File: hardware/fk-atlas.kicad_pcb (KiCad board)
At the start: 2 copper layers, 88.4 x 80.3 mm, 127 parts, among them J1 CONN-HDR-2x5, J2 MICRO-USB, J201 CONN_01X02, J3 Conn_01x02, J301 CONN_01X02, J4 Conn_01x07, J401 CONN_01X02, J501 CONN_01X02, J601 CONN_01X02, P2 ATLAS_EC_PROBE, P3 ATLAS_RTD_PROBE, P4 ATLAS_PH_PROBE, P5 ATLAS_DO_PROBE, P6 ATLAS_ORP_PROBE, Q1 2N7002LT1G, Q2 2N7002LT1G, Q3 2N7002LT1G, Q4 2N7002LT1G, Q5 2N7002LT1G, SW1 SPNO, U1 S25FL1xxK0XM, U2 ATSAMD21G18A-AU, U201 ADM3260, U202 ATLAS_EC, U3 MCP1700T-3302E/MB, U301 ADM3260, U302 ATLAS_RTD, U401 ADM3260, U402 ATLAS_PH, U501 ADM3260, U502 ATLAS_DO, U601 ADM3260, U602 ATLAS_ORP, Y1 FC-135

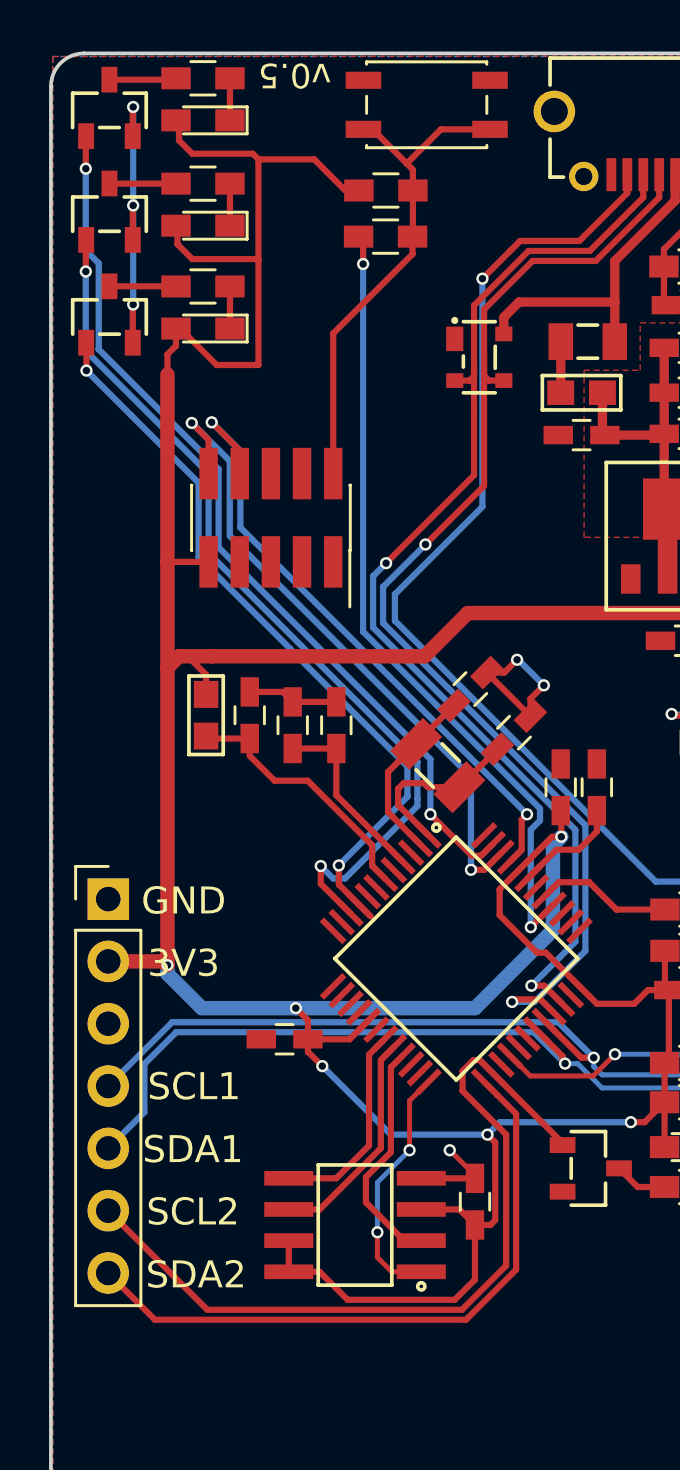
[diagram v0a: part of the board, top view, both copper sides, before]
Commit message: Break out Wire3 instead of Wire2.
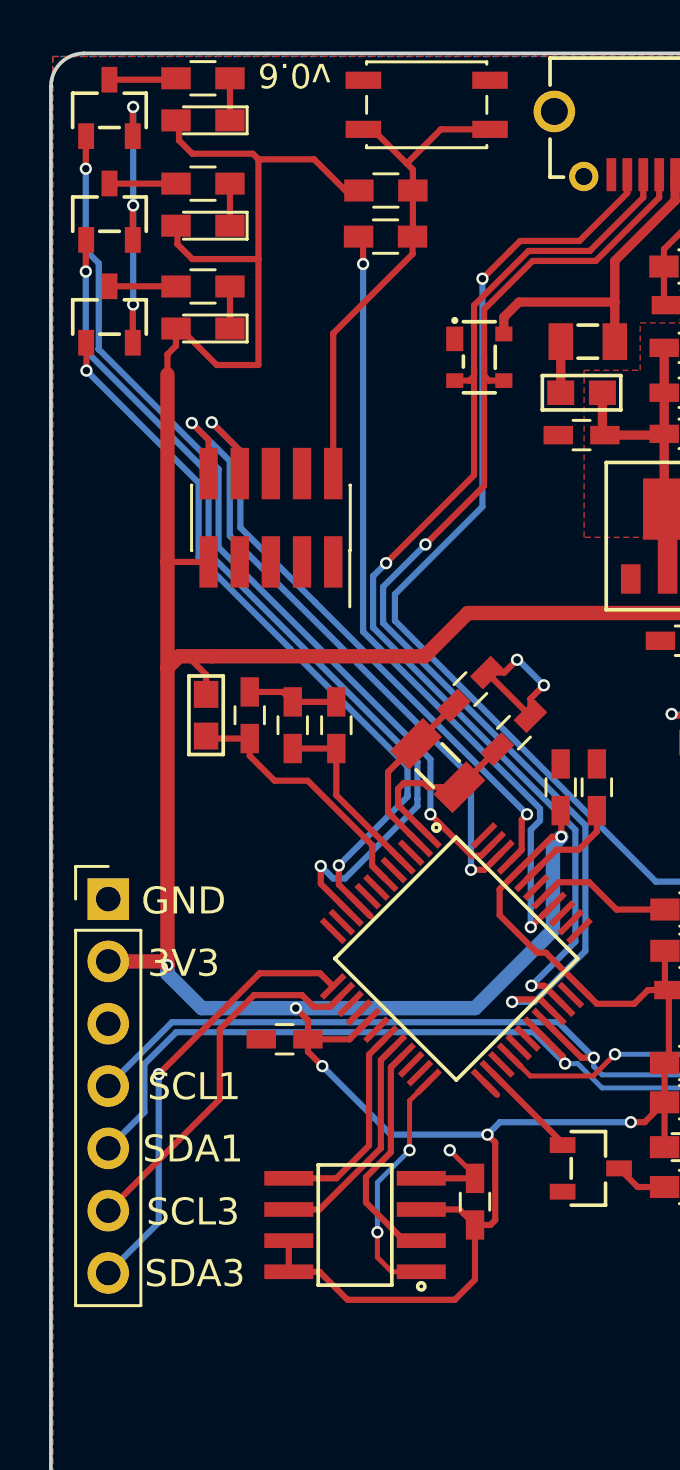
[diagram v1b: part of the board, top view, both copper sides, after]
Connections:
- net /D5 renamed /FLASH_CS
- net /SCL renamed /SCL1
- net /SDA renamed /SDA1
- J4 pad 6: /D13 -> /SCL3
- J4 pad 7: /D11 -> /SDA3
- U2 pad 13: /D4 -> /SDA3
- U2 pad 14: /D3 -> /SCL3
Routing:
- net /D13: track 33.0 -> 4.11 mm
- net /D11: track 26.5 -> 0.75 mm
- net /SDA3: track 0.00 -> 18.0 mm, vias 0 -> 1
- net /SCL3: track 0.00 -> 15.2 mm
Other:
- board text added: "SCL3"
- board text added: "SDA3"
- board text added: "v0.6"
- board text removed: "SCL2"
- board text removed: "SDA2"
- board text removed: "v0.5"

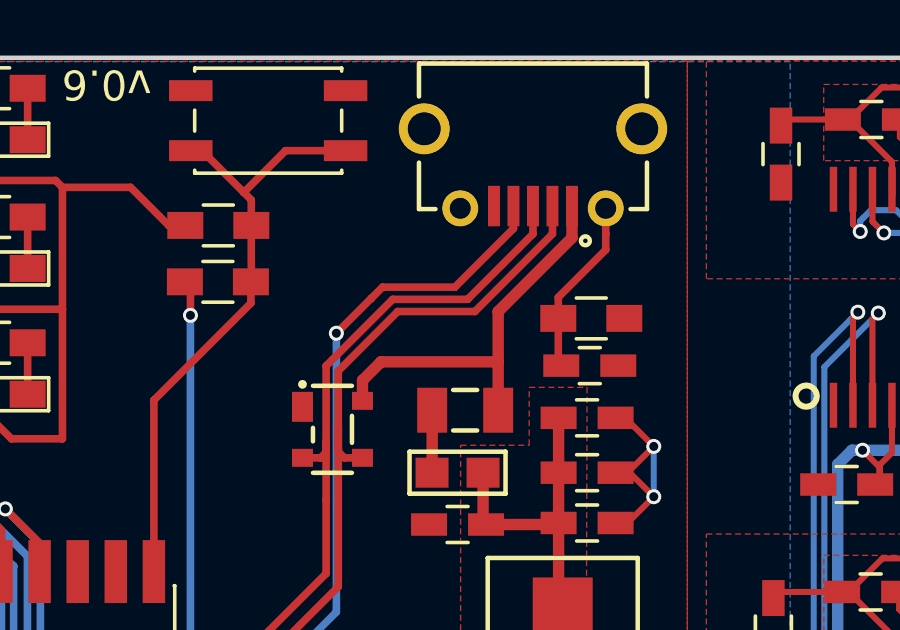
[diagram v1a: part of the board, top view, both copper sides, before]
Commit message: Give GND on USB a firmer connection.
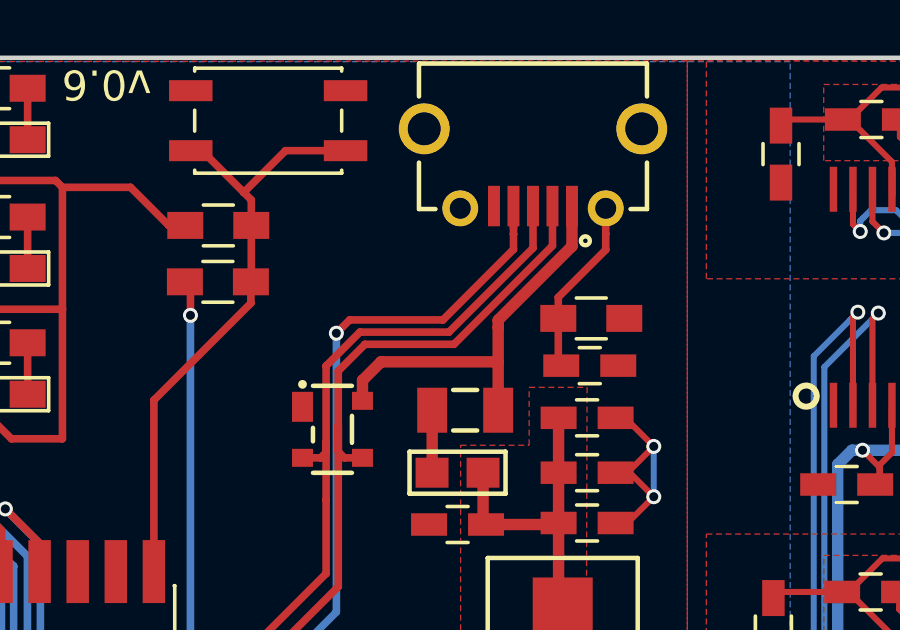
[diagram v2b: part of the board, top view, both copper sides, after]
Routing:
- net Net-(J2-Pad4): track 43.9 -> 45.1 mm
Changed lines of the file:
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@@
     (links 348)
     (no_connects 0)
-    (area 115.672799 57.328999 204.214801 137.743001)
+    (area 106.559933 55.6511 223.731401 137.9054)
     (thickness 1.6)
     (drawings 25)
-    (tracks 1150)
+    (tracks 1152)
     (zones 0)
     (modules 127)
@@
   )
   (setup
-    (last_trace_width 0.254)
+    (last_trace_width 0.381)
     (user_trace_width 0.203)
     (user_trace_width 0.381)
@@
   (segment (start 123.0454 64.4271) (end 123.0454 62.4381) (width 0.254) (layer F.Cu) (net 56))
   (segment (start 123.0454 60.1345) (end 123.0454 58.42) (width 0.254) (layer F.Cu) (net 57))
+  (segment (start 139.8905 62.3465) (end 139.8905 63.746597) (width 0.254) (layer F.Cu) (net 58))
+  (segment (start 139.8905 63.746597) (end 137.089107 66.54799) (width 0.254) (layer F.Cu) (net 58))
+  (segment (start 137.089107 66.54799) (end 134.12146 66.54799) (width 0.254) (layer F.Cu) (net 58))
+  (segment (start 134.12146 66.54799) (end 132.99439 67.67506) (width 0.254) (layer F.Cu) (net 58))
+  (segment (start 132.99439 67.67506) (end 132.99439 70.2056) (width 0.254) (layer F.Cu) (net 58))
   (segment (start 135.3312 95.4024) (end 137.123309 93.610291) (width 0.254) (layer B.Cu) (net 58))
   (segment (start 137.123309 93.610291) (end 137.123309 89.050559) (width 0.254) (layer B.Cu) (net 58))
@@
   (segment (start 135.850273 95.4024) (end 135.3312 95.4024) (width 0.254) (layer F.Cu) (net 58))
   (via (at 135.3312 95.4024) (size 0.5) (drill 0.3) (layers F.Cu B.Cu) (net 58))
-  (segment (start 132.99439 67.67506) (end 132.99439 70.2056) (width 0.254) (layer F.Cu) (net 58))
   (segment (start 132.99439 70.2056) (end 132.99439 72.13599) (width 0.254) (layer F.Cu) (net 58))
   (segment (start 132.207 70.739) (end 132.811 70.739) (width 0.254) (layer F.Cu) (net 58))
@@
   (segment (start 132.99439 74.59582) (end 129.40901 78.1812) (width 0.254) (layer F.Cu) (net 58))
   (via (at 129.40901 78.1812) (size 0.5) (drill 0.3) (layers F.Cu B.Cu) (net 58))
-  (segment (start 139.8905 62.3465) (end 139.8905 63.2755) (width 0.254) (layer F.Cu) (net 58))
-  (segment (start 139.8905 63.2755) (end 137.71021 65.45579) (width 0.254) (layer F.Cu) (net 58))
-  (segment (start 137.71021 65.45579) (end 135.213659 65.455791) (width 0.254) (layer F.Cu) (net 58))
-  (segment (start 135.213659 65.455791) (end 132.99439 67.67506) (width 0.254) (layer F.Cu) (net 58))
+  (segment (start 140.5405 62.3465) (end 140.5405 63.671347) (width 0.254) (layer F.Cu) (net 59))
+  (segment (start 140.5405 63.671347) (end 137.257448 66.9544) (width 0.254) (layer F.Cu) (net 59))
+  (segment (start 137.257448 66.9544) (end 134.2898 66.9544) (width 0.254) (layer F.Cu) (net 59))
+  (segment (start 134.2898 66.9544) (end 133.4008 67.8434) (width 0.254) (layer F.Cu) (net 59))
+  (segment (start 133.4008 67.8434) (end 133.4008 69.6722) (width 0.254) (layer F.Cu) (net 59))
   (segment (start 131.0132 77.4192) (end 129.28602 79.14638) (width 0.254) (layer B.Cu) (net 59))
   (segment (start 137.529719 88.863319) (end 137.529719 93.987395) (width 0.254) (layer B.Cu) (net 59))
@@
   (via (at 134.5438 96.0628) (size 0.5) (drill 0.3) (layers F.Cu B.Cu) (net 59))
   (segment (start 133.4008 75.0316) (end 133.4008 69.6722) (width 0.254) (layer F.Cu) (net 59))
-  (segment (start 133.4008 69.6722) (end 133.4008 67.8434) (width 0.254) (layer F.Cu) (net 59))
   (segment (start 134.207 70.739) (end 133.603 70.739) (width 0.254) (layer F.Cu) (net 59))
   (segment (start 133.603 70.739) (end 133.4008 70.5368) (width 0.254) (layer F.Cu) (net 59))
   (segment (start 133.4008 70.5368) (end 133.4008 69.6722) (width 0.254) (layer F.Cu) (net 59))
   (segment (start 131.0132 77.4192) (end 133.4008 75.0316) (width 0.254) (layer F.Cu) (net 59))
-  (segment (start 133.4008 67.8434) (end 135.382 65.8622) (width 0.254) (layer F.Cu) (net 59))
-  (segment (start 140.5405 63.2755) (end 140.5405 62.3465) (width 0.254) (layer F.Cu) (net 59))
-  (segment (start 135.382 65.8622) (end 137.9538 65.8622) (width 0.254) (layer F.Cu) (net 59))
-  (segment (start 137.9538 65.8622) (end 140.5405 63.2755) (width 0.254) (layer F.Cu) (net 59))
   (via (at 131.0132 77.4192) (size 0.5) (drill 0.3) (layers F.Cu B.Cu) (net 59))
+  (segment (start 141.1905 62.3465) (end 141.1905 63.6859) (width 0.381) (layer F.Cu) (net 60))
+  (segment (start 141.1905 63.6859) (end 138.7299 66.1465) (width 0.381) (layer F.Cu) (net 60))
+  (segment (start 138.7299 66.1465) (end 138.7299 66.3956) (width 0.381) (layer F.Cu) (net 60))
+  (segment (start 138.7299 66.3956) (end 138.7299 67.5386) (width 0.381) (layer F.Cu) (net 60))
   (segment (start 134.207 68.158) (end 134.8264 67.5386) (width 0.381) (layer F.Cu) (net 60))
-  (segment (start 138.7299 65.8631) (end 138.7299 67.5386) (width 0.381) (layer F.Cu) (net 60))
   (segment (start 138.7299 67.5386) (end 138.7299 69.1515) (width 0.381) (layer F.Cu) (net 60))
   (segment (start 134.8264 67.5386) (end 138.7299 67.5386) (width 0.381) (layer F.Cu) (net 60))
   (segment (start 134.207 68.839) (end 134.207 68.158) (width 0.381) (layer F.Cu) (net 60))
-  (segment (start 141.1905 62.3465) (end 141.1905 63.4025) (width 0.381) (layer F.Cu) (net 60))
-  (segment (start 141.1905 63.4025) (end 138.7299 65.8631) (width 0.381) (layer F.Cu) (net 60))
   (segment (start 136.5299 69.1515) (end 136.5299 71.2303) (width 0.381) (layer F.Cu) (net 61))
   (segment (start 136.5299 71.2303) (end 136.5259 71.2343) (width 0.381) (layer F.Cu) (net 61))
@@
   (segment (start 128.859 60.4995) (end 130.2512 61.8917) (width 0.254) (layer F.Cu) (net 65))
   (segment (start 130.2512 64.858) (end 130.2376 64.8716) (width 0.254) (layer F.Cu) (net 65))
+  (segment (start 133.335982 66.584782) (end 133.779184 66.14158) (width 0.254) (layer F.Cu) (net 66))
+  (segment (start 133.779184 66.14158) (end 136.89007 66.14158) (width 0.254) (layer F.Cu) (net 66))
+  (segment (start 136.89007 66.14158) (end 139.2405 63.79115) (width 0.254) (layer F.Cu) (net 66))
+  (segment (start 139.2405 63.79115) (end 139.2405 63.2755) (width 0.254) (layer F.Cu) (net 66))
+  (segment (start 139.2405 62.3465) (end 139.2405 63.2755) (width 0.254) (layer F.Cu) (net 66))
+  (segment (start 139.2405 63.2755) (end 139.2428 63.2778) (width 0.254) (layer F.Cu) (net 66))
   (segment (start 142.9512 91.1606) (end 140.40175 91.1606) (width 0.254) (layer B.Cu) (net 66))
   (segment (start 140.40175 91.1606) (end 129.7686 80.52745) (width 0.254) (layer B.Cu) (net 66))
@@
   (segment (start 129.7686 79.447314) (end 133.335982 75.879932) (width 0.254) (layer B.Cu) (net 66))
   (segment (start 133.335982 75.879932) (end 133.335982 66.584782) (width 0.254) (layer B.Cu) (net 66))
-  (segment (start 133.335982 66.584782) (end 134.490364 65.4304) (width 0.254) (layer F.Cu) (net 66))
-  (segment (start 134.490364 65.4304) (end 134.492982 65.4304) (width 0.254) (layer F.Cu) (net 66))
-  (segment (start 134.492982 65.4304) (end 134.874 65.049382) (width 0.254) (layer F.Cu) (net 66))
-  (segment (start 134.874 65.049382) (end 137.287018 65.049382) (width 0.254) (layer F.Cu) (net 66))
-  (segment (start 137.287018 65.049382) (end 139.2405 63.0959) (width 0.254) (layer F.Cu) (net 66))
   (segment (start 139.2405 63.0959) (end 139.2405 62.3465) (width 0.254) (layer F.Cu) (net 66))
   (via (at 133.335982 66.584782) (size 0.5) (drill 0.3) (layers F.Cu B.Cu) (net 66))

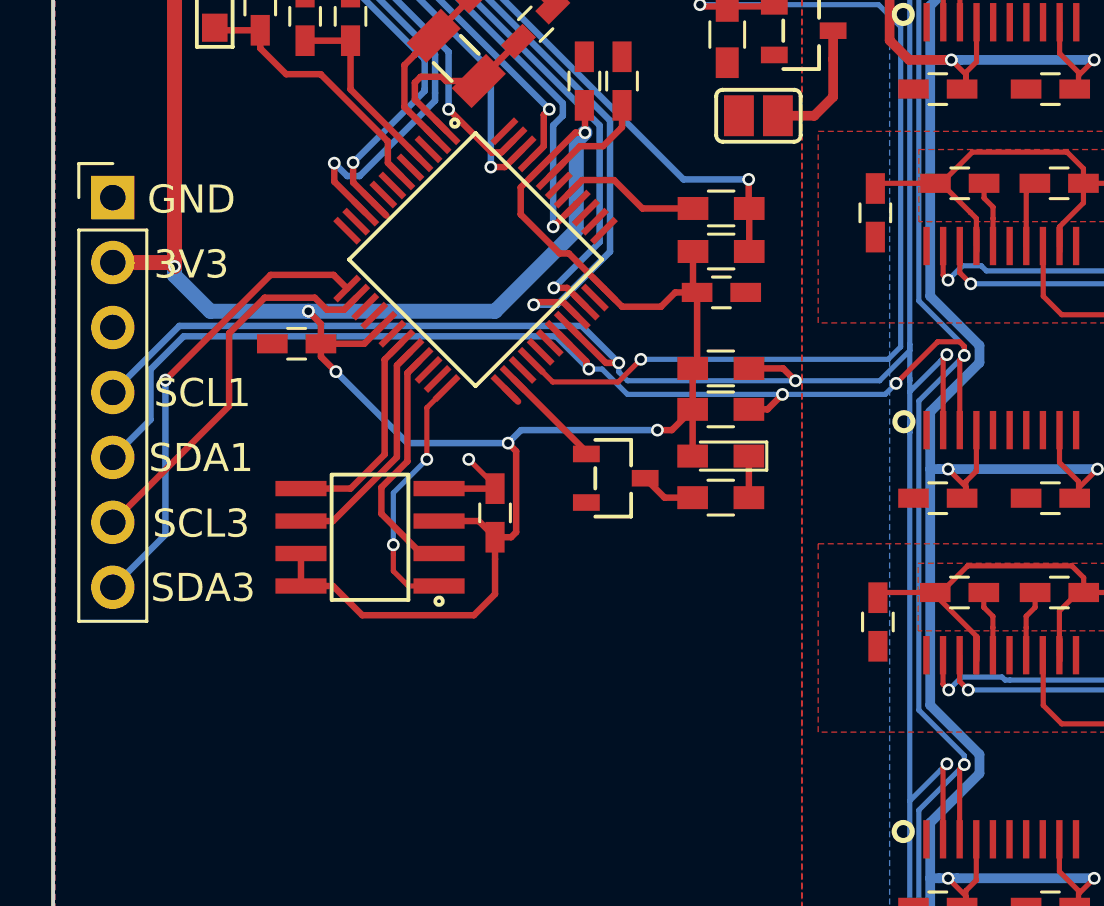
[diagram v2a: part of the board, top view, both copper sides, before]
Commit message: Break out D30/D31 serial lines.
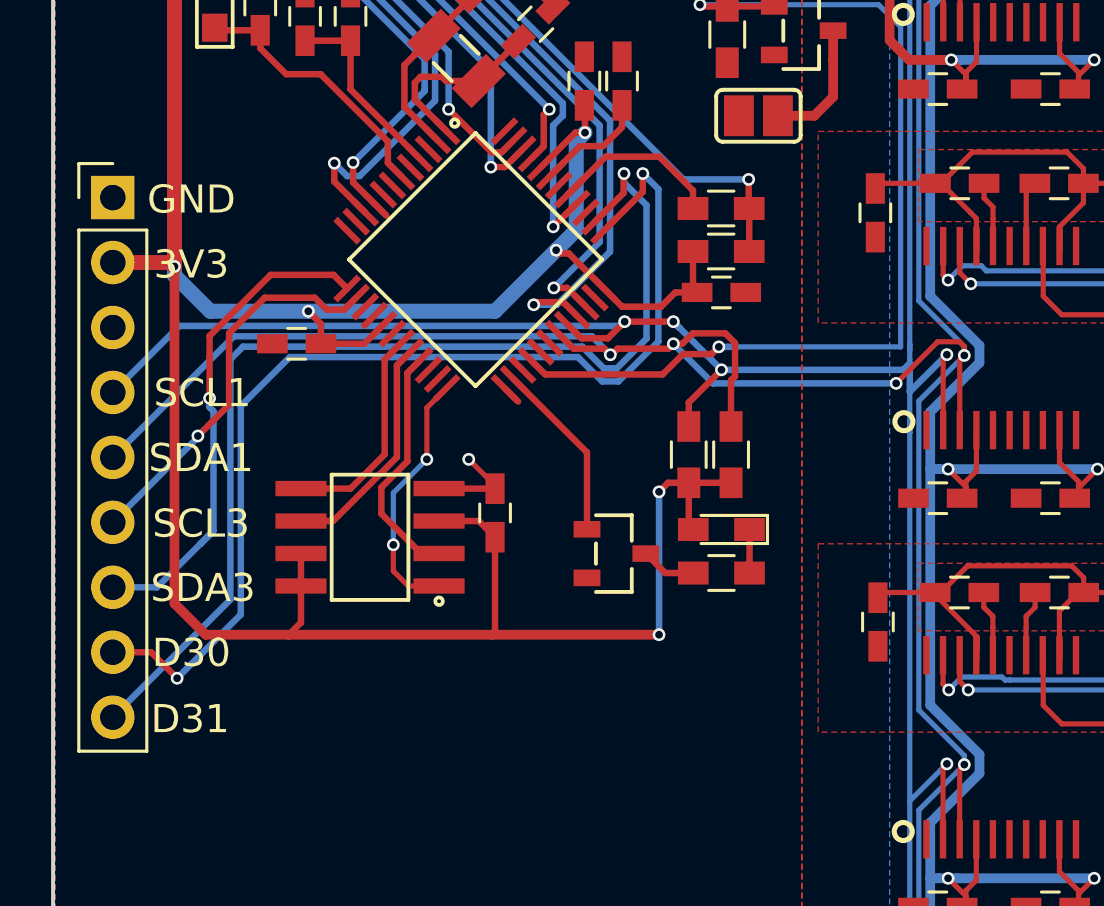
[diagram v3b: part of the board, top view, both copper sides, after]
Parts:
- J4: value Conn_01x07 -> Conn_01x09; footprint Socket_Strips:Socket_Strip_Straight_1x07_Pitch2.54mm -> Socket_Strips:Socket_Strip_Straight_1x09_Pitch2.54mm
- moved R4 3.60 mm to (140.6, 101.9), turned to 90 degrees
- moved Q4 2.95 mm to (137.8, 105.8)
- moved R11 2.95 mm to (141.9, 106.6)
- moved D4 2.87 mm to (141.9, 104.9)
- moved R5 1.82 mm to (142.3, 101.9), turned to 90 degrees
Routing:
- net /D30: track 0.00 -> 42.5 mm, vias 0 -> 2
- net /D31: track 0.00 -> 42.4 mm, vias 0 -> 1
- net +3V3: track 330.2 -> 336.5 mm
- net /SDA1: track 128.1 -> 131.6 mm
- net /D13: track 4.11 -> 7.07 mm
- net /SDA3: track 18.0 -> 19.7 mm
- net /USB_ID: track 5.84 -> 7.56 mm
- net /SCL1: track 126.7 -> 128.4 mm, vias 7 -> 8
- net /SCL3: vias 0 -> 1
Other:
- board text added: "D30"
- board text added: "D31"
